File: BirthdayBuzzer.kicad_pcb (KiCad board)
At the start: 2 copper layers, 39.9 x 33.1 mm, 15 parts, among them J3 Conn_ARM_SWD_TagConnect_TC203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, SW1 SW_Push, U1 PIC18F15Q41-I/SS

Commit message: Added Github QR-Code to desgin
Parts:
- added G***: LOGO, LOGO, F.Cu at (90.0, 62.4)
- moved G*** 9.00 mm to (89.5, 50.0)
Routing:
- net GND: track 1.38 -> 6.64 mm, vias 2 -> 6
- added copper zone on F.Cu, net GND

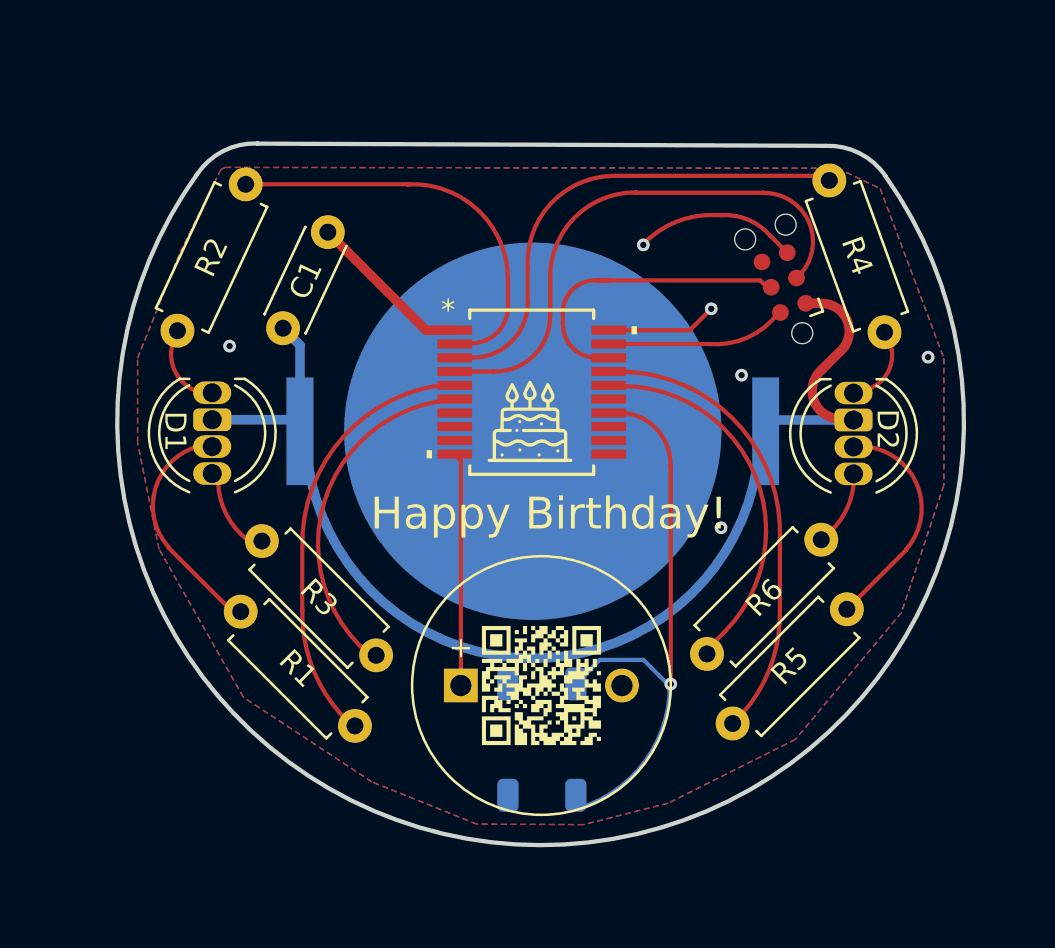
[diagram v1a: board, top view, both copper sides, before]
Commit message: Fixed Capacitor in Schematics and GND in layout
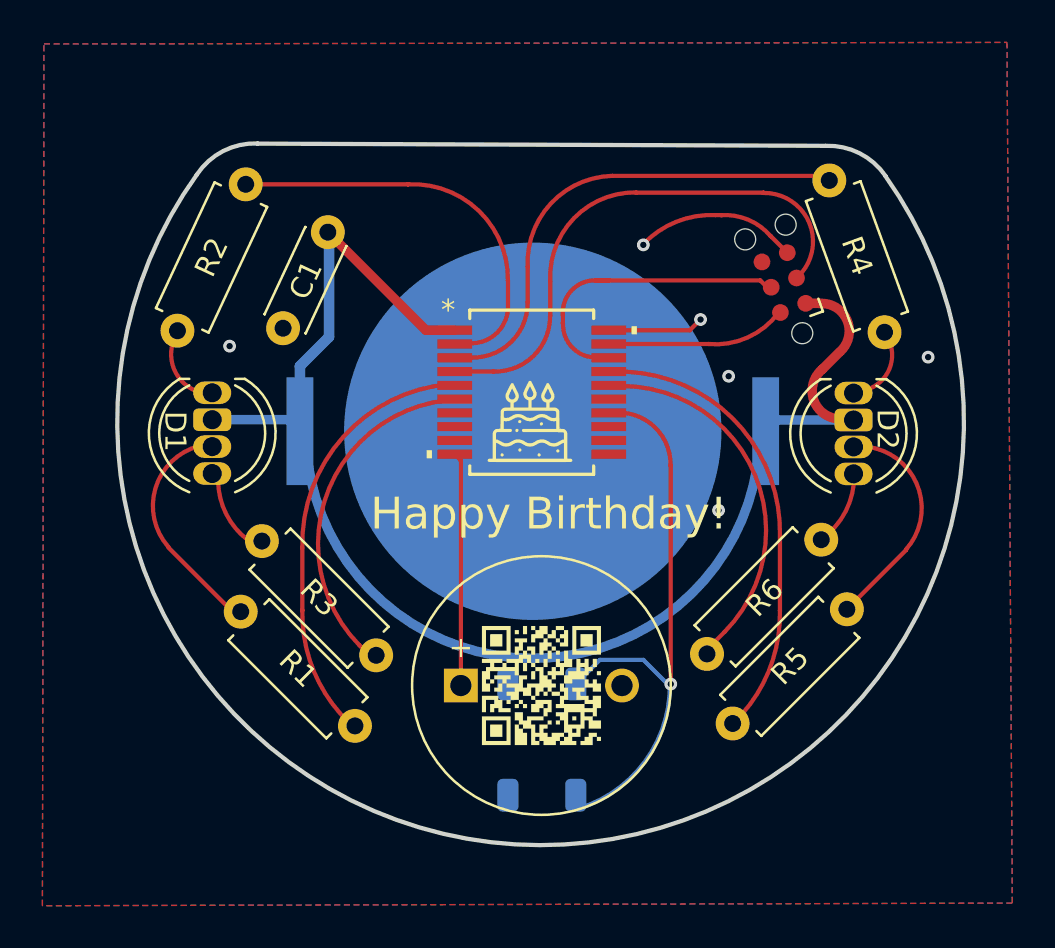
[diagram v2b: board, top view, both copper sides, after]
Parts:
- C1: value C -> 10uF
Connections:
- BT1 pad 1: +3V0 -> +3V6
- C1 pad 1: +3V0 -> GND
- C1 pad 2: Net-(U1-VDD) -> +3V6
- D1 pad 4: +3V0 -> +3V6
- D2 pad 4: +3V0 -> +3V6
- J3 pad 1: +3V0 -> +3V6
- U1 pad 1: Net-(U1-VDD) -> +3V6
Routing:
- net +3V6: track 0.00 -> 31.3 mm
- net +3V0: track 19.0 -> 0.00 mm
- net Net-(U1-VDD): track 7.90 -> 0.00 mm
